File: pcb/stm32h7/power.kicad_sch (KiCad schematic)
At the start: 15 parts, among them J1 USB_C_Receptacle_USB2.0_14P, J2 Battery, U10 MAX17048G_T10, U2 NCP186AMX330TAG, U3 USBLC6-2SC6, U4 MCP73831-2-OT, U7 DMG3415U-7

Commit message: is it finally done or am i going insane
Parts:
- added D4: MBR0540, Diode_SMD:D_SOD-123, symbol Diode:MBR0540
- added Q2: IRLML2244, Package_TO_SOT_SMD:SOT-23, symbol Transistor_FET:DMG3414U
- added R11: 10k, Resistor_SMD:R_0402_1005Metric, symbol Device:R_US
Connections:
- net +3V3: now also Q2.3 (D); no longer C12.2, U2.1 (OUT), U2.2 (OUT__1), U2.4 (FB/ADJ)
- new net BTN: D4.1 (K)
- new net LDO_OUT: C12.2, Q2.2 (S), R11.2, U2.1 (OUT), U2.2 (OUT__1), U2.4 (FB/ADJ)
- new net PWR_ON: D4.2 (A), Q2.1 (G), R11.1
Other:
- note added: "Main Power Switch"

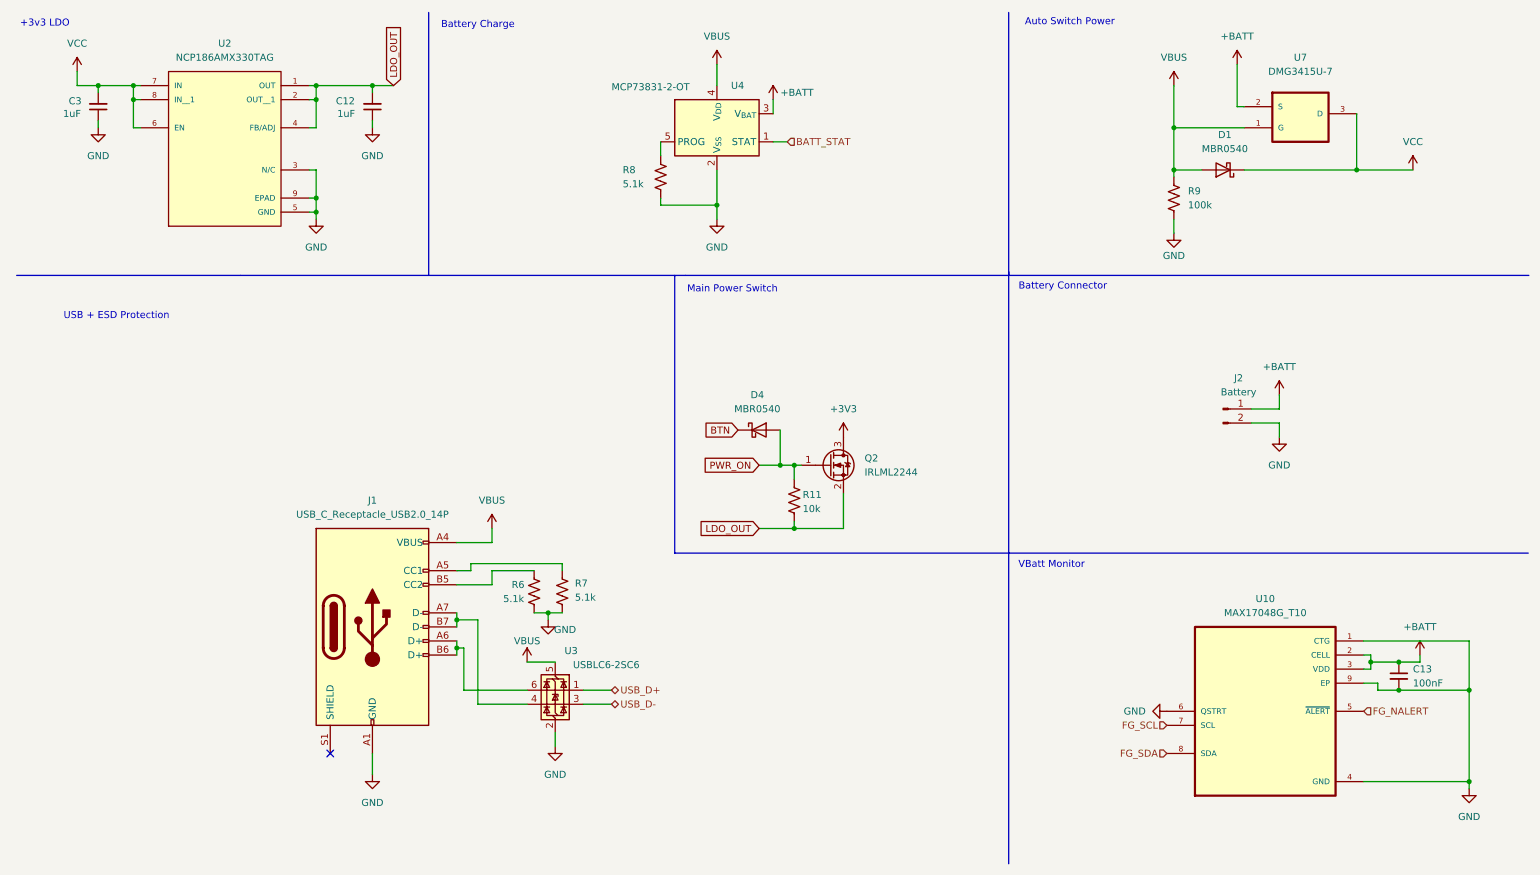
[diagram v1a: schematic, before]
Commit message: using EN on the LDO for power switch now
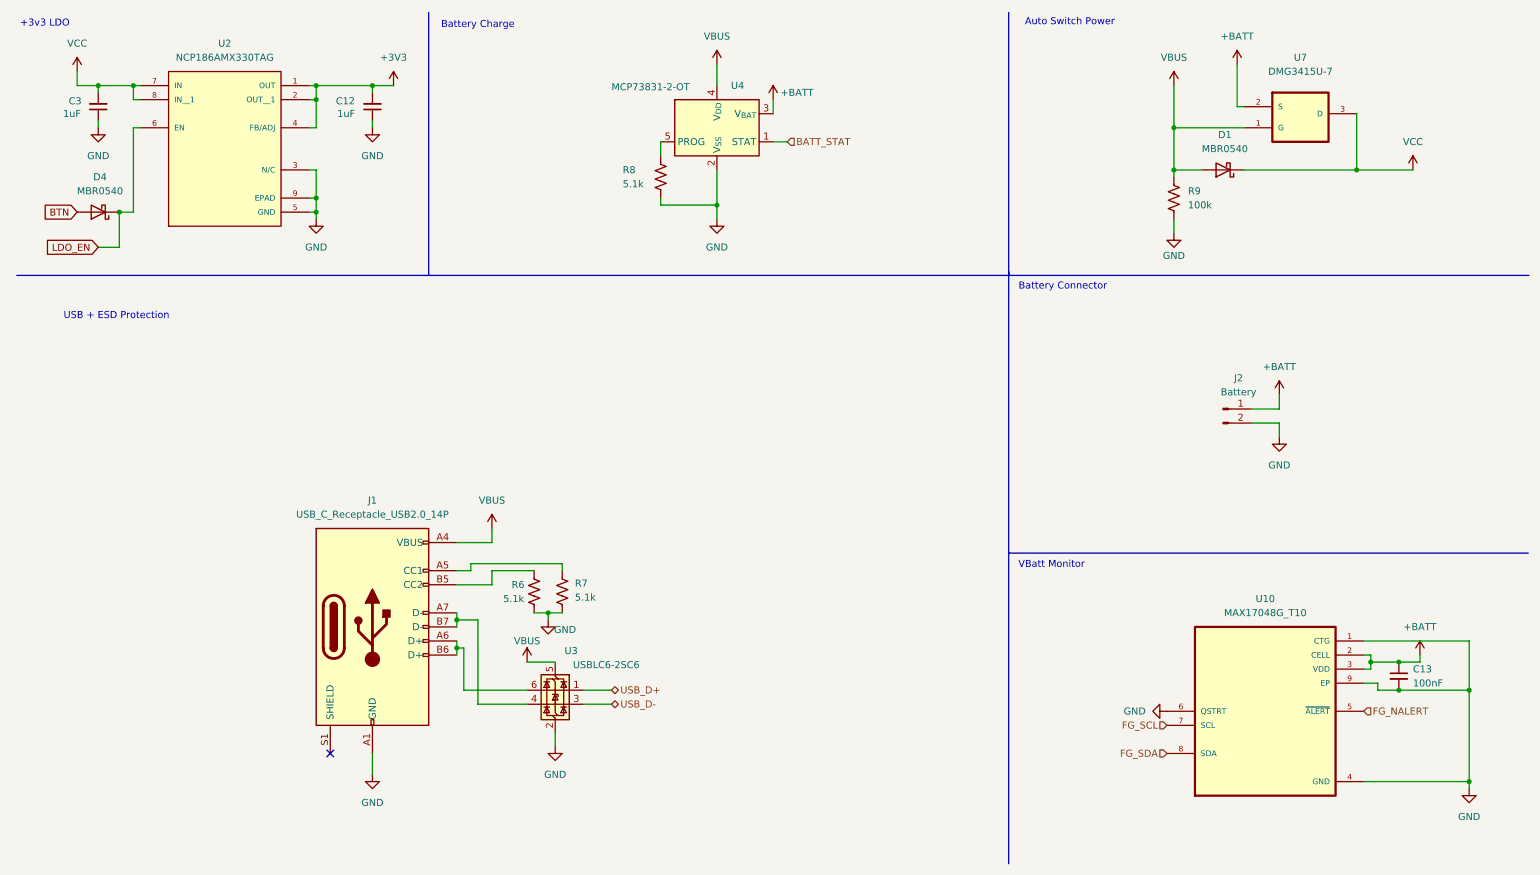
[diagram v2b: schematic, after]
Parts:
- removed Q2: IRLML2244, Package_TO_SOT_SMD:SOT-23, symbol Transistor_FET:DMG3414U
- removed R11: 10k, Resistor_SMD:R_0402_1005Metric, symbol Device:R_US
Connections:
- net LDO_OUT is gone; now on net +3V3: C12.2, U2.1 (OUT), U2.2 (OUT__1), U2.4 (FB/ADJ)
- net PWR_ON is gone; now on net BTN: D4.2 (A)
- net BTN: no longer D4.1 (K)
- net VCC: no longer U2.6 (EN)
- new net LDO_EN: D4.1 (K), U2.6 (EN)
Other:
- note removed: "Main Power Switch"

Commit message: fixed some wiring
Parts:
- added R11: 0R, Resistor_SMD:R_0402_1005Metric, symbol Device:R_US
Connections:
- net LDO_EN: now also R11.1
- net VCC: now also R11.2
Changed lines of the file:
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@@
 	(paper "A4")
 	(junction
+		(at 31.75 48.26)
+		(diameter 0)
+		(color 0 0 0 0)
+	)
+	(junction
 		(at 261.62 134.62)
 		(diameter 0)
@@
 	)
 	(junction
-		(at 66.04 27.94)
+		(at 31.75 54.61)
 		(diameter 0)
 		(color 0 0 0 0)
 	)
 	(junction
-		(at 33.02 25.4)
+		(at 66.04 27.94)
 		(diameter 0)
 		(color 0 0 0 0)
 	)
 	(junction
-		(at 30.48 48.26)
+		(at 33.02 25.4)
 		(diameter 0)
 		(color 0 0 0 0)
@@
 	(wire
 		(pts
-			(xy 26.67 54.61) (xy 30.48 54.61)
+			(xy 26.67 54.61) (xy 31.75 54.61)
 		)
 		(stroke
@@
 	(wire
 		(pts
+			(xy 31.75 54.61) (xy 31.75 57.15)
+		)
+		(stroke
+			(width 0)
+			(type default)
+		)
+	)
+	(wire
+		(pts
 			(xy 255.27 130.81) (xy 256.54 130.81)
 		)
@@
 	(wire
 		(pts
-			(xy 30.48 48.26) (xy 30.48 54.61)
+			(xy 31.75 48.26) (xy 31.75 54.61)
 		)
 		(stroke
@@
 	(wire
 		(pts
-			(xy 33.02 48.26) (xy 30.48 48.26)
+			(xy 33.02 48.26) (xy 31.75 48.26)
 		)
 		(stroke
@@
 	(polyline
 		(pts
-			(xy 86.36 12.192) (xy 86.36 59.69)
+			(xy 86.36 12.192) (xy 86.36 75.565)
 		)
 		(stroke
@@
 	(wire
 		(pts
+			(xy 31.75 48.26) (xy 30.48 48.26)
+		)
+		(stroke
+			(width 0)
+			(type default)
+		)
+	)
+	(wire
+		(pts
 			(xy 66.04 45.72) (xy 66.04 48.26)
 		)
@@
 	(polyline
 		(pts
-			(xy 11.938 59.69) (xy 52.451 59.69)
+			(xy 12.192 75.565) (xy 86.36 75.565)
 		)
 		(stroke
@@
 		)
 	)
-	(polyline
-		(pts
-			(xy 52.451 59.69) (xy 132.715 59.69)
-		)
-		(stroke
-			(width 0)
-			(type default)
-		)
-	)
 	(wire
 		(pts
@@
 	(text "USB + ESD Protection"
 		(exclude_from_sim no)
-		(at 29.972 67.056 0)
+		(at 23.622 96.52 0)
 		(effects
 			(font
@@
 	)
 	(symbol
+		(lib_id "Device:R_US")
+		(at 31.75 60.96 0)
+		(unit 1)
+		(exclude_from_sim no)
+		(in_bom yes)
+		(on_board yes)
+		(dnp yes)
+		(property "Reference" "R11"
+			(at 24.892 59.69 0)
+			(effects
+				(font
+					(size 1.27 1.27)
+				)
+				(justify left)
+			)
+		)
+		(property "Value" "0R"
+			(at 24.892 62.23 0)
+			(effects
+				(font
+					(size 1.27 1.27)
+				)
+				(justify left)
+			)
+		)
+		(property "Footprint" "Resistor_SMD:R_0402_1005Metric"
+			(at 32.766 61.214 90)
+			(effects
+				(font
+					(size 1.27 1.27)
+				)
+				(hide yes)
+			)
+		)
+		(property "Datasheet" "~"
+			(at 31.75 60.96 0)
+			(effects
+				(font
+					(size 1.27 1.27)
+				)
+				(hide yes)
+			)
+		)
+		(property "Description" "Resistor, US symbol"
+			(at 31.75 60.96 0)
+			(effects
+				(font
+					(size 1.27 1.27)
+				)
+				(hide yes)
+			)
+		)
+		(pin "2"
+		)
+		(pin "1"
+		)
+		(instances
+			(project "stm32h7"
+				(path "/834edf73-57a5-43b4-ab36-0b077e93e6d5/ae5309e0-349d-45c3-b1b4-6edffcac73ca"
+					(reference "R11")
+					(unit 1)
+				)
+			)
+		)
+	)
+	(symbol
 		(lib_id "power:+BATT")
 		(at 148.59 27.94 0)
@@
 					(unit 1)
 				)
+			)
+		)
+	)
+	(symbol
+		(lib_id "power:VCC")
+		(at 31.75 64.77 180)
+		(unit 1)
+		(exclude_from_sim no)
+		(in_bom yes)
+		(on_board yes)
+		(dnp no)
+		(fields_autoplaced yes)
+		(property "Reference" "#PWR082"
+			(at 31.75 60.96 0)
+			(effects
+				(font
+					(size 1.27 1.27)
+				)
+				(hide yes)
+			)
+		)
+		(property "Value" "VCC"
+			(at 31.75 69.85 0)
+			(effects
+				(font
+					(size 1.27 1.27)
+				)
+			)
+		)
+		(property "Footprint" ""
+			(at 31.75 64.77 0)
+			(effects
+				(font
+					(size 1.27 1.27)
+				)
+				(hide yes)
+			)
+		)
+		(property "Datasheet" ""
+			(at 31.75 64.77 0)
+			(effects
+				(font
+					(size 1.27 1.27)
+				)
+				(hide yes)
+			)
+		)
+		(property "Description" "Power symbol creates a global label with name \"VCC\""
+			(at 31.75 64.77 0)
+			(effects
+				(font
+					(size 1.27 1.27)
+				)
+				(hide yes)
+			)
+		)
+		(pin "1"
+		)
+		(instances
+			(project "stm32h7"
+				(path "/834edf73-57a5-43b4-ab36-0b077e93e6d5/ae5309e0-349d-45c3-b1b4-6edffcac73ca"
+					(reference "#PWR082")
+					(unit 1)
+				)
